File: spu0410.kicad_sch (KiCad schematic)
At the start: 10 parts, among them U1601 LT6233CS6#TRMPBF

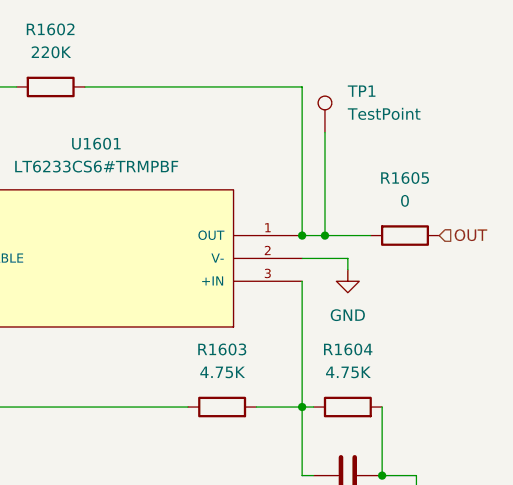
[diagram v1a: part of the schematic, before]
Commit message: Schematic Changes
Added Manufacturer/MPN/Description Fields to parts
Added libraries to project
Modified FMC schematic to use new symbol
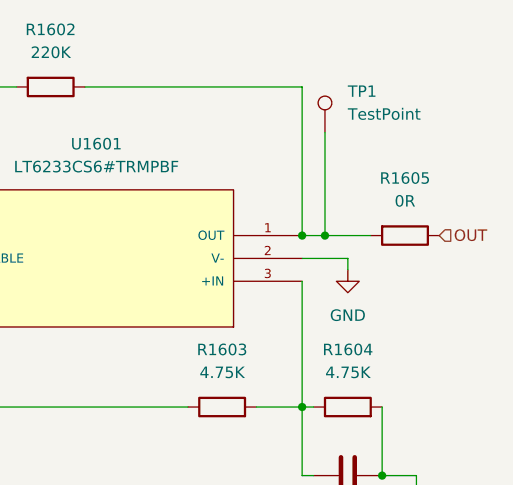
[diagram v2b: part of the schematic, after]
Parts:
- C1601, C1602: Manufacturer (none) -> Murata; Manufacturer Part Number (none) -> GRM188R61E105KA12D
- MIC1601: Manufacturer (none) -> Knowles; Manufacturer Part Number (none) -> SPU0410HR5H-PB
- R1601, R1603, R1604: Manufacturer (none) -> YAGEO; Manufacturer Part Number (none) -> RC0603FR-074K75L
- R1602: Manufacturer (none) -> YAGEO; Manufacturer Part Number (none) -> RC0603FR-07220KL
- R1605: value 0 -> 0R; Manufacturer (none) -> Panasonic; Manufacturer Part Number (none) -> ERJ-3GEY0R00V
- U1601: Manufacturer (none) -> Analog Devices; Manufacturer Part Number (none) -> LT6233CS6#TRMPBF
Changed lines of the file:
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@@
 			)
 		)
-		(property "Value" "0"
+		(property "Value" "0R"
 			(at 215.9 67.31 90)
 			(effects
@@
 			)
 		)
-		(property "Description" "Resistor"
+		(property "Description" "RES SMD 0 OHM JUMPER 1/10W 0603"
 			(at 215.9 71.12 0)
 			(effects
@@
 		(property "Vendor" "digikey:P0.0GCT-ND"
 			(at 144.78 -144.78 0)
+			(effects
+				(font
+					(size 1.27 1.27)
+				)
+				(hide yes)
+			)
+		)
+		(property "Manufacturer" "Panasonic"
+			(at 215.9 71.12 0)
+			(effects
+				(font
+					(size 1.27 1.27)
+				)
+				(hide yes)
+			)
+		)
+		(property "Manufacturer Part Number" "ERJ-3GEY0R00V "
+			(at 215.9 71.12 0)
 			(effects
 				(font
@@
 			)
 		)
-		(property "Description" "Resistor"
+		(property "Description" "RES 220K OHM 1% 1/10W 0603"
 			(at 176.53 54.61 0)
 			(effects
@@
 		(property "Vendor" "digikey:311-220KHRCT-ND"
 			(at 121.92 -121.92 0)
+			(effects
+				(font
+					(size 1.27 1.27)
+				)
+				(hide yes)
+			)
+		)
+		(property "Manufacturer" "YAGEO "
+			(at 176.53 54.61 0)
+			(effects
+				(font
+					(size 1.27 1.27)
+				)
+				(hide yes)
+			)
+		)
+		(property "Manufacturer Part Number" "RC0603FR-07220KL "
+			(at 176.53 54.61 0)
 			(effects
 				(font
@@
 			)
 		)
-		(property "Description" "Unpolarized capacitor"
+		(property "Description" "CAP CER 1UF 25V X5R 0603"
 			(at 209.55 97.79 0)
 			(effects
@@
 		(property "Vendor" "digikey:490-3897-1-ND"
 			(at 307.34 -111.76 0)
+			(effects
+				(font
+					(size 1.27 1.27)
+				)
+				(hide yes)
+			)
+		)
+		(property "Manufacturer" "Murata"
+			(at 209.55 97.79 0)
+			(effects
+				(font
+					(size 1.27 1.27)
+				)
+				(hide yes)
+			)
+		)
+		(property "Manufacturer Part Number" "GRM188R61E105KA12D"
+			(at 209.55 97.79 0)
 			(effects
 				(font
@@
 			)
 		)
-		(property "Description" "Resistor"
+		(property "Description" "RES 4.75K OHM 1% 1/10W 0603"
 			(at 195.58 90.17 0)
 			(effects
@@
 		(property "Vendor" "digikey:311-4.75KHRCT-ND"
 			(at 285.75 285.75 0)
+			(effects
+				(font
+					(size 1.27 1.27)
+				)
+				(hide yes)
+			)
+		)
+		(property "Manufacturer" "YAGEO "
+			(at 195.58 90.17 0)
+			(effects
+				(font
+					(size 1.27 1.27)
+				)
+				(hide yes)
+			)
+		)
+		(property "Manufacturer Part Number" "RC0603FR-074K75L "
+			(at 195.58 90.17 0)
 			(effects
 				(font
@@
 			)
 		)
-		(property "Description" "Unpolarized capacitor"
+		(property "Description" "CAP CER 1UF 25V X5R 0603"
 			(at 118.11 76.2 0)
 			(effects
@@
 		(property "Vendor" "digikey:490-3897-1-ND"
 			(at 41.91 -41.91 0)
+			(effects
+				(font
+					(size 1.27 1.27)
+				)
+				(hide yes)
+			)
+		)
+		(property "Manufacturer" "Murata"
+			(at 118.11 76.2 0)
+			(effects
+				(font
+					(size 1.27 1.27)
+				)
+				(hide yes)
+			)
+		)
+		(property "Manufacturer Part Number" "GRM188R61E105KA12D"
+			(at 118.11 76.2 0)
 			(effects
 				(font
@@
 			)
 		)
+		(property "Manufacturer" ""
+			(at 207.01 59.69 0)
+			(effects
+				(font
+					(size 1.27 1.27)
+				)
+				(hide yes)
+			)
+		)
+		(property "Manufacturer Part Number" ""
+			(at 207.01 59.69 0)
+			(effects
+				(font
+					(size 1.27 1.27)
+				)
+				(hide yes)
+			)
+		)
 		(pin "1"
 		)
@@
 			)
 		)
-		(property "Description" "Resistor"
+		(property "Description" "RES 4.75K OHM 1% 1/10W 0603"
 			(at 125.73 76.2 0)
 			(effects
@@
 		(property "Vendor" "digikey:311-4.75KHRCT-ND"
 			(at 49.53 -49.53 0)
+			(effects
+				(font
+					(size 1.27 1.27)
+				)
+				(hide yes)
+			)
+		)
+		(property "Manufacturer" "YAGEO "
+			(at 125.73 76.2 0)
+			(effects
+				(font
+					(size 1.27 1.27)
+				)
+				(hide yes)
+			)
+		)
+		(property "Manufacturer Part Number" "RC0603FR-074K75L "
+			(at 125.73 76.2 0)
 			(effects
 				(font
@@
 			)
 		)
-		(property "Description" ""
+		(property "Description" "IC OPAMP GP 1 CIRCUIT TSOT23-6"
 			(at 204.47 71.12 0)
 			(effects
@@
 		(property "Vendor" "digikey:LT6233CS6#TRMPBFCT-ND"
 			(at 408.94 142.24 0)
+			(effects
+				(font
+					(size 1.27 1.27)
+				)
+				(hide yes)
+			)
+		)
+		(property "Manufacturer" "Analog Devices"
+			(at 204.47 71.12 0)
+			(effects
+				(font
+					(size 1.27 1.27)
+				)
+				(hide yes)
+			)
+		)
+		(property "Manufacturer Part Number" "LT6233CS6#TRMPBF "
+			(at 204.47 71.12 0)
 			(effects
 				(font
@@
 			)
 		)
-		(property "Description" ""
+		(property "Description" "MIC MEMS ANALOG OMNI -42DB"
 			(at 73.66 76.2 0)
 			(effects
@@
 		(property "Vendor" "digikey:423-1138-1-ND"
 			(at 0 152.4 0)
+			(effects
+				(font
+					(size 1.27 1.27)
+				)
+				(hide yes)
+			)
+		)
+		(property "Manufacturer" "Knowles "
+			(at 73.66 76.2 0)
+			(effects
+				(font
+					(size 1.27 1.27)
+				)
+				(hide yes)
+			)
+		)
+		(property "Manufacturer Part Number" "SPU0410HR5H-PB "
+			(at 73.66 76.2 0)
 			(effects
 				(font
@@
 			)
 		)
-		(property "Description" "Resistor"
+		(property "Description" "RES 4.75K OHM 1% 1/10W 0603"
 			(at 209.55 90.17 0)
 			(effects
@@
 			(effects
 				(font
+					(size 1.27 1.27)
+				)
+				(hide yes)
+			)
+		)
+		(property "Manufacturer" "YAGEO "
+			(at 209.55 90.17 0)
+			(effects
+				(font
+					(size 1.27 1.27)
+				)
+				(hide yes)
+			)
+		)
+		(property "Manufacturer Part Number" "RC0603FR-074K75L "
+			(at 209.55 90.17 0)
+			(effects
+				(font

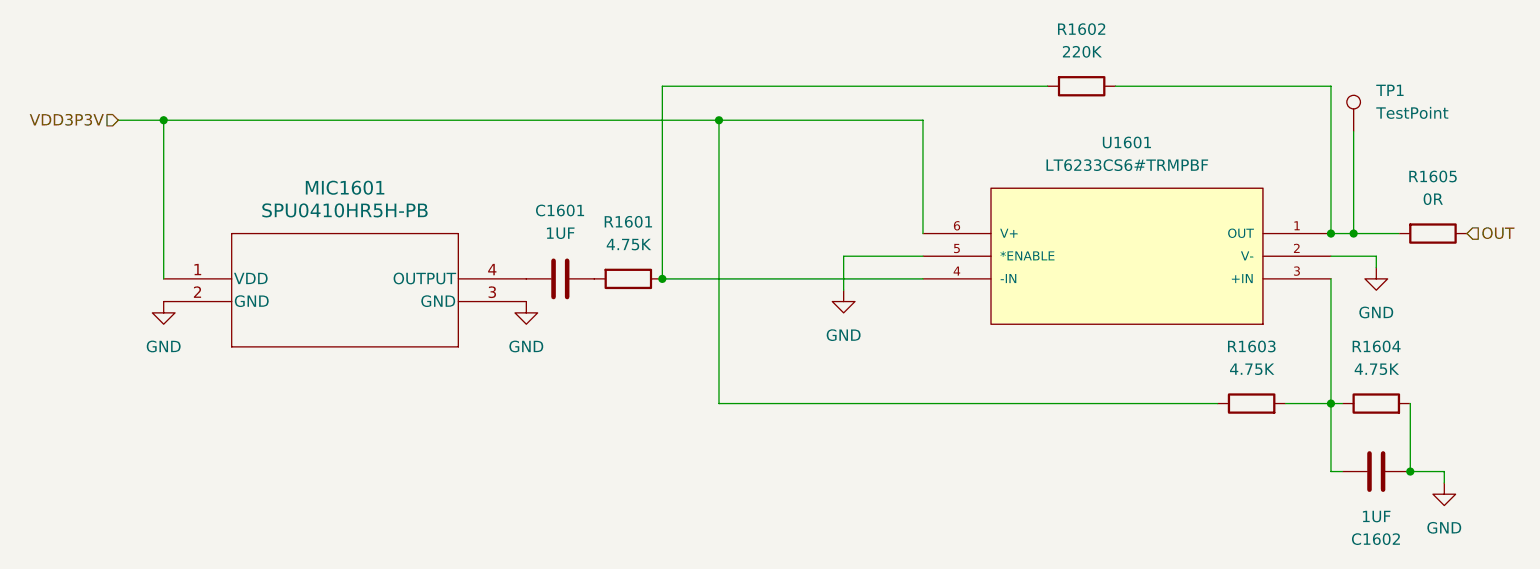
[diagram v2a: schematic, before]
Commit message: Schematics update
Cleaned up RF ADC and front end sections.
Verified that changes did not changes anything about the layout.
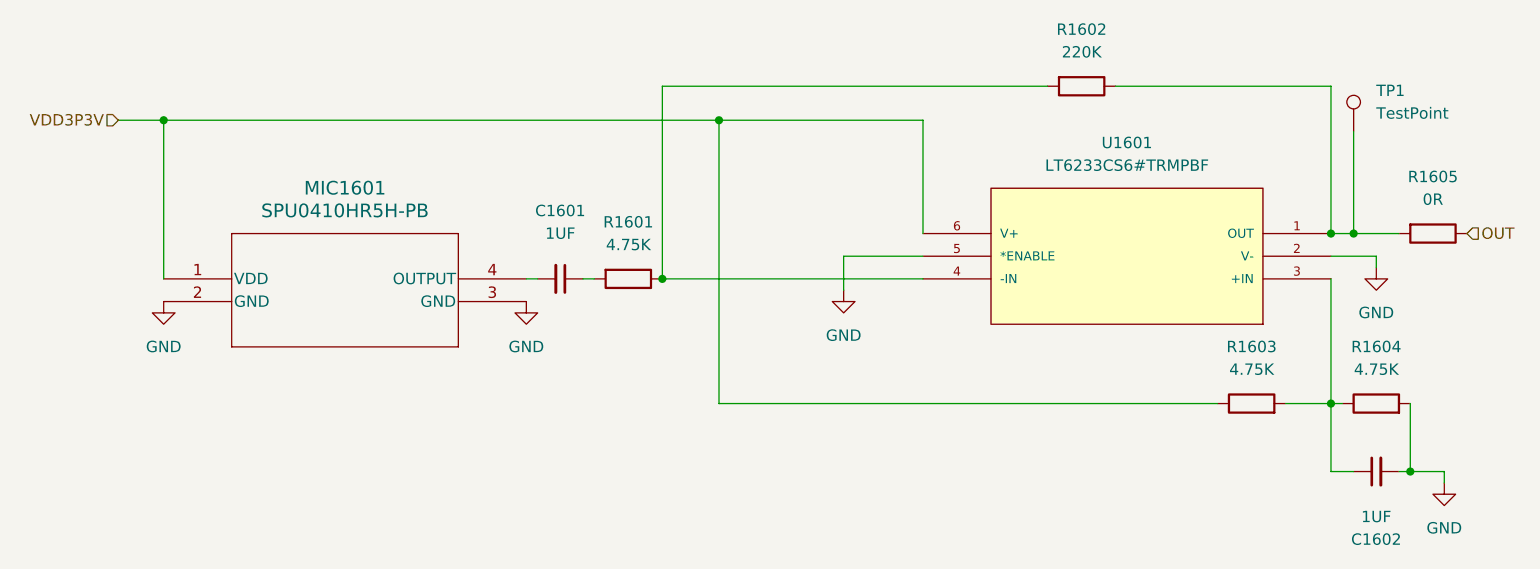
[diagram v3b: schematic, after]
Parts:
- C1601, C1602: symbol Device:C -> Device:C_Small
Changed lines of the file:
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@@
+	)
+	(junction
+		(at 129.54 76.2)
+		(diameter 0)
+		(color 0 0 0 0)
+	)
+	(junction
+		(at 73.66 58.42)
+		(diameter 0)
+		(color 0 0 0 0)
 	)
 	(junction
@@
 	)
 	(junction
-		(at 129.54 76.2)
-		(diameter 0)
-		(color 0 0 0 0)
-	)
-	(junction
-		(at 73.66 58.42)
-		(diameter 0)
-		(color 0 0 0 0)
-	)
-	(junction
 		(at 207.01 71.12)
 		(diameter 0)
@@
 	(wire
 		(pts
+			(xy 114.3 76.2) (xy 115.57 76.2)
+		)
+		(stroke
+			(width 0)
+			(type default)
+		)
+	)
+	(wire
+		(pts
 			(xy 209.55 73.66) (xy 209.55 74.93)
 		)
@@
 	(wire
 		(pts
+			(xy 212.09 97.79) (xy 213.36 97.79)
+		)
+		(stroke
+			(width 0)
+			(type default)
+		)
+	)
+	(wire
+		(pts
 			(xy 73.66 58.42) (xy 135.89 58.42)
 		)
@@
 	(wire
 		(pts
-			(xy 204.47 97.79) (xy 205.74 97.79)
+			(xy 204.47 97.79) (xy 207.01 97.79)
 		)
 		(stroke
@@
 		(pts
 			(xy 129.54 76.2) (xy 158.75 76.2)
+		)
+		(stroke
+			(width 0)
+			(type default)
+		)
+	)
+	(wire
+		(pts
+			(xy 120.65 76.2) (xy 121.92 76.2)
 		)
 		(stroke
@@
 	)
 	(symbol
-		(lib_id "Device:C")
+		(lib_id "Device:C_Small")
 		(at 209.55 97.79 90)
 		(mirror x)
@@
 	)
 	(symbol
-		(lib_id "Device:C")
+		(lib_id "Device:C_Small")
 		(at 118.11 76.2 270)
 		(unit 1)

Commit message: Properly attributed DNP parts; Added Fabrication Notes
-Properly attributed various DNP in the project;
This includes: C210.C710,C1601,C2502,C2602,L2501,R1507,L2601,R1601,R805
- I changed the accelerometer and microphone (+it's filter)to DNP parts
  Note: both of these are obsolete parts. As part of this change I Changed R1602 (part of mic buffer) from 220k to 0R. The removal of these parts should in no way negatively effect the rest of the circuit.
-I fixed the 'value' attribute of XMER2501&XMER2601 from 'TC4-6+' -> 'TC4-6T+'
- I added some fabrication notes to the F.Fab Layer
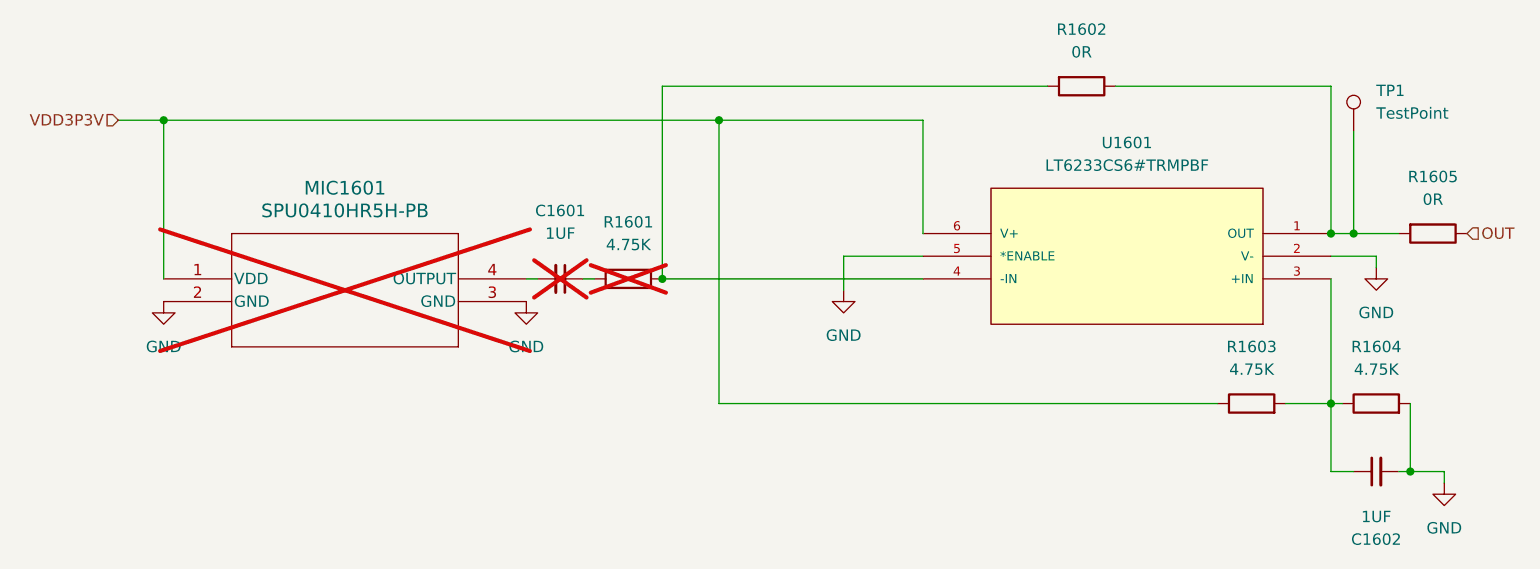
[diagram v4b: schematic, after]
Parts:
- C1601, MIC1601, R1601: now not fitted
- R1602: value 220K -> 0R; Manufacturer YAGEO -> Panasonic; Manufacturer Part Number RC0603FR-07220KL -> ERJ-3GEY0R00V; Vendor digikey:311-220KHRCT-ND -> digikey:P0.0GCT-ND
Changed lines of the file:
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@@
 			)
 		)
-		(property "Value" "220K"
+		(property "Value" "0R"
 			(at 176.53 50.8 90)
 			(effects
@@
 			)
 		)
-		(property "Description" "RES 220K OHM 1% 1/10W 0603"
+		(property "Description" "RES SMD 0 OHM JUMPER 1/10W 0603"
 			(at 176.53 54.61 0)
 			(effects
@@
 			)
 		)
-		(property "Vendor" "digikey:311-220KHRCT-ND"
+		(property "Vendor" "digikey:P0.0GCT-ND"
 			(at 121.92 -121.92 0)
 			(effects
@@
 			)
 		)
-		(property "Manufacturer" "YAGEO "
+		(property "Manufacturer" "Panasonic"
 			(at 176.53 54.61 0)
 			(effects
@@
 			)
 		)
-		(property "Manufacturer Part Number" "RC0603FR-07220KL "
+		(property "Manufacturer Part Number" "ERJ-3GEY0R00V "
 			(at 176.53 54.61 0)
 			(effects
@@
 		(in_bom yes)
 		(on_board yes)
-		(dnp no)
+		(dnp yes)
 		(fields_autoplaced yes)
 		(property "Reference" "C1601"
@@
 		(in_bom yes)
 		(on_board yes)
-		(dnp no)
+		(dnp yes)
 		(fields_autoplaced yes)
 		(property "Reference" "R1601"
@@
 		(in_bom yes)
 		(on_board yes)
-		(dnp no)
+		(dnp yes)
 		(fields_autoplaced yes)
 		(property "Reference" "MIC1601"
